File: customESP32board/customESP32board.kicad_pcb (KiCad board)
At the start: 2 copper layers, 60 x 65 mm, 49 parts, among them J1 USB_B, J2 Conn_01x16_Pin, J3 Conn_01x16_Pin, Q1 S8050, Q2 S8050, Q3 BSS138, Q4 BSS138, Q5 BSS138, SW1 SW_Push, SW2 SW_Push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

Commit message: updated ibom according do latest bom (sent to production line)
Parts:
- C1: value 10uF/25V -> 10uF, 25V
- C3: value 0.1uF -> 0.1uF, 10V
- C6: value 0.1uF, 10v -> 0.1uF, 10V
- C7: value 10uF, 10v -> 10uF, 25V
- R10, R7, R8, R9: value 220 Ohm, 1/4 Watt -> 200 Ohm, 1/4 Watt
- R13, R14, R15: value 220 Ohm -> 200 Ohm, 1/4 Watt
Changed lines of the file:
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@@
 			)
 		)
-		(property "Value" "10uF, 10v"
+		(property "Value" "10uF, 25V"
 			(at 0 1.68 0)
 			(layer "F.Fab")
@@
 			)
 		)
-		(property "Value" "10uF/25V"
+		(property "Value" "10uF, 25V"
 			(at 0 1.68 0)
 			(layer "F.Fab")
@@
 			)
 		)
-		(property "Value" "220 Ohm, 1/4 Watt"
+		(property "Value" "200 Ohm, 1/4 Watt"
 			(at 0 1.43 90)
 			(layer "F.Fab")
@@
 			)
 		)
-		(property "Value" "220 Ohm"
+		(property "Value" "200 Ohm, 1/4 Watt"
 			(at 0 1.43 90)
 			(layer "F.Fab")
@@
 			)
 		)
-		(property "Value" "0.1uF"
+		(property "Value" "0.1uF, 10V"
 			(at 0 1.43 90)
 			(layer "F.Fab")
@@
 			)
 		)
-		(property "Value" "0.1uF, 10v"
+		(property "Value" "0.1uF, 10V"
 			(at 0 1.43 0)
 			(layer "F.Fab")
@@
 			)
 		)
-		(property "Value" "220 Ohm, 1/4 Watt"
+		(property "Value" "200 Ohm, 1/4 Watt"
 			(at 0 1.43 90)
 			(layer "F.Fab")
@@
 			)
 		)
-		(property "Value" "220 Ohm"
+		(property "Value" "200 Ohm, 1/4 Watt"
 			(at 0 1.43 90)
 			(layer "F.Fab")
@@
 			)
 		)
-		(property "Value" "220 Ohm, 1/4 Watt"
+		(property "Value" "200 Ohm, 1/4 Watt"
 			(at 0 1.43 90)
 			(layer "F.Fab")
@@
 			)
 		)
-		(property "Value" "220 Ohm, 1/4 Watt"
+		(property "Value" "200 Ohm, 1/4 Watt"
 			(at 0 1.43 90)
 			(layer "F.Fab")
@@
 			)
 		)
-		(property "Value" "220 Ohm"
+		(property "Value" "200 Ohm, 1/4 Watt"
 			(at 0 1.43 90)
 			(layer "F.Fab")
@@
 			)
 		)
-		(property "link" "https://uge-one.com/product/smd-micro-push-button-switch-2p-3x4x2mm/"
+		(property "link" "https://uge-one.com/product/smd-micro-switch-white-tact-s-3-6-5-2-pin/"
 			(at 0 0 90)
 			(unlocked yes)

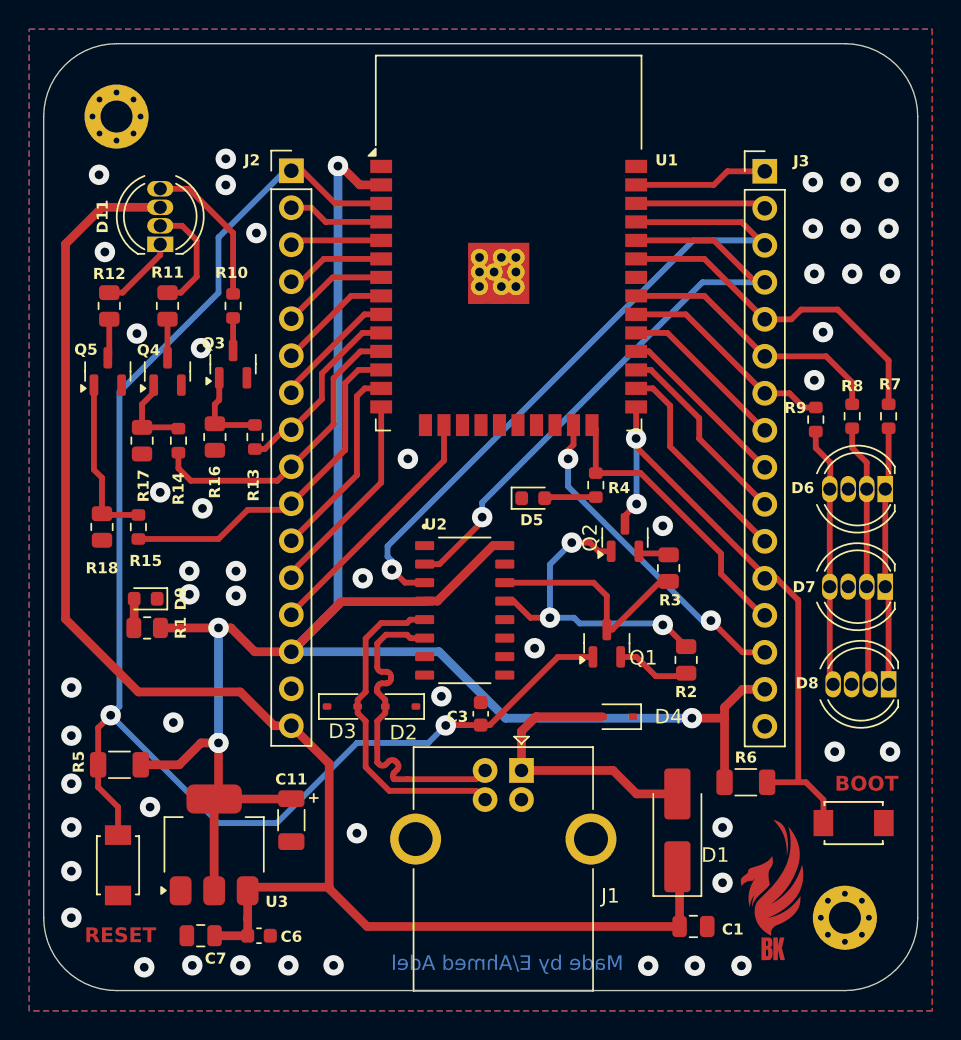
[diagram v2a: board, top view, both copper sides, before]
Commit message: update layout routing and placement after schematic changes
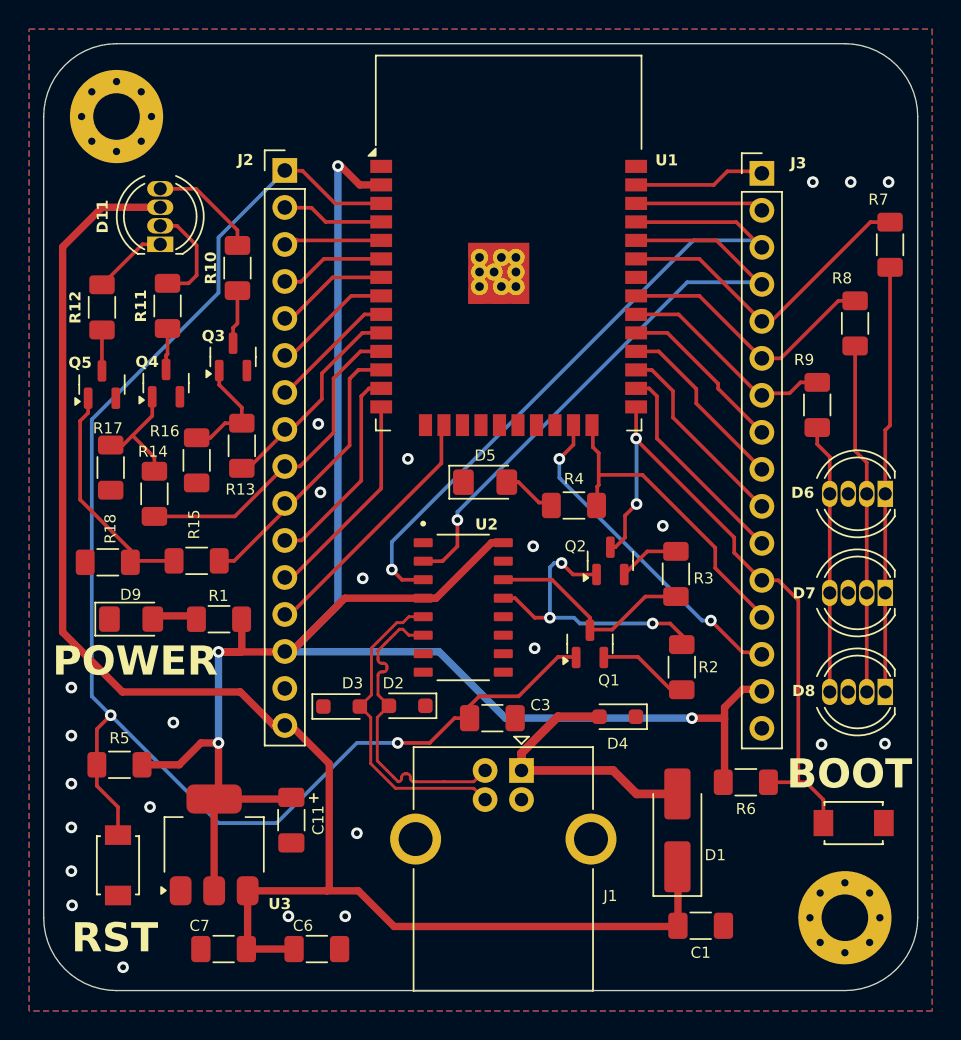
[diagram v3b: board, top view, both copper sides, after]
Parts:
- removed G***: LOGO, LOGO
- C1, C7: footprint Capacitor_SMD:C_0805_2012Metric -> Capacitor_SMD:C_1206_3216Metric_Pad1.33x1.80mm_HandSolder
- C11: footprint Capacitor_SMD:C_1206_3216Metric -> Capacitor_SMD:C_1206_3216Metric_Pad1.33x1.80mm_HandSolder
- C3, C6: footprint Capacitor_SMD:C_0603_1608Metric -> Capacitor_SMD:C_1206_3216Metric_Pad1.33x1.80mm_HandSolder
- D2, D3, D4: footprint Diode_SMD:D_SOD-323 -> Diode_SMD:D_SOD-323_HandSoldering
- D5, D9: footprint LED_SMD:LED_0603_1608Metric -> LED_SMD:LED_1206_3216Metric_Pad1.42x1.75mm_HandSolder
- H1, H2: footprint MountingHole:MountingHole_2.2mm_M2_Pad_Via -> MountingHole:MountingHole_3.2mm_M3_Pad_Via
- R1, R11, R12, R16, R17, R18, R2, R3: footprint Resistor_SMD:R_0805_2012Metric -> Resistor_SMD:R_1206_3216Metric_Pad1.30x1.75mm_HandSolder
- R10, R13, R14, R15, R9: value 200 Ohm, 1/4 Watt -> 220 Ohm; footprint Resistor_SMD:R_0603_1608Metric -> Resistor_SMD:R_1206_3216Metric_Pad1.30x1.75mm_HandSolder
- R4: footprint Resistor_SMD:R_0603_1608Metric -> Resistor_SMD:R_1206_3216Metric_Pad1.30x1.75mm_HandSolder
- R5, R6: value 10 Ohm -> 10k Ohm; footprint Resistor_SMD:R_1206_3216Metric -> Resistor_SMD:R_1206_3216Metric_Pad1.30x1.75mm_HandSolder
- R7, R8: value 200 Ohm, 1/4 Watt -> 130 Ohm; footprint Resistor_SMD:R_0603_1608Metric -> Resistor_SMD:R_1206_3216Metric_Pad1.30x1.75mm_HandSolder
- moved R7 11.8 mm to (162.6, 87.3)
- moved R8 6.38 mm to (160.2, 92.7)
- moved R1 4.97 mm to (116.5, 113.0)
- moved R15 4.63 mm to (115.0, 109.0), turned to 0 degrees
- moved C6 4.07 mm to (123.2, 135.7)
- moved R14 4.01 mm to (112.1, 104.4)
- moved D5 3.48 mm to (134.8, 103.6)
- moved R17 2.84 mm to (109.1, 102.6)
- moved R10 2.62 mm to (117.8, 88.9)
- moved R18 2.46 mm to (108.9, 109.1), turned to 180 degrees
- moved R4 2.05 mm to (140.9, 105.2), turned to 0 degrees
- moved R16 2.03 mm to (115.0, 102.1)
- moved Q2 1.89 mm to (143.4, 109.0)
- moved C7 1.82 mm to (116.8, 135.7)
- moved D9 1.72 mm to (110.5, 113.0), turned to 0 degrees
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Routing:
- net RGB_BLUE: track 17.8 -> 29.3 mm
- net RGB_GREEN: track 18.1 -> 24.1 mm
- net ESP_IO27: track 24.2 -> 19.5 mm
- net Net-(Q5-G): track 11.6 -> 16.0 mm
- net Net-(D11-RK): track 10.4 -> 7.53 mm
- net +5V: track 104.4 -> 107.1 mm
- net ESP_IO0: track 43.0 -> 45.4 mm
- net Net-(Q4-G): track 5.77 -> 8.06 mm
- net Net-(Q2-B): track 2.15 -> 4.21 mm
- net ESP_IO2: track 19.9 -> 21.9 mm
- net +3V3: track 135.0 -> 133.2 mm
- net ESP_IO21: track 23.8 -> 22.0 mm
- net Net-(Q3-G): track 6.06 -> 7.77 mm
- net ESP_IO26: track 20.9 -> 22.4 mm
- net ESP_IO25: track 13.0 -> 14.6 mm
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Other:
- board text added: "POWER"
- board text added: "RST"
- board text removed: "RESET"
